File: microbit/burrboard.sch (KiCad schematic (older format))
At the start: 15 parts, among them J1 SENSORS, J2 microbit_edge_connector, J4 SPI, J6 3v3, J7 Conn_01x06, J8 I2C, J9 GND, Q1 Q_Photo_NPN, SW1 POWER_SW, U1 TMP36GT9Z

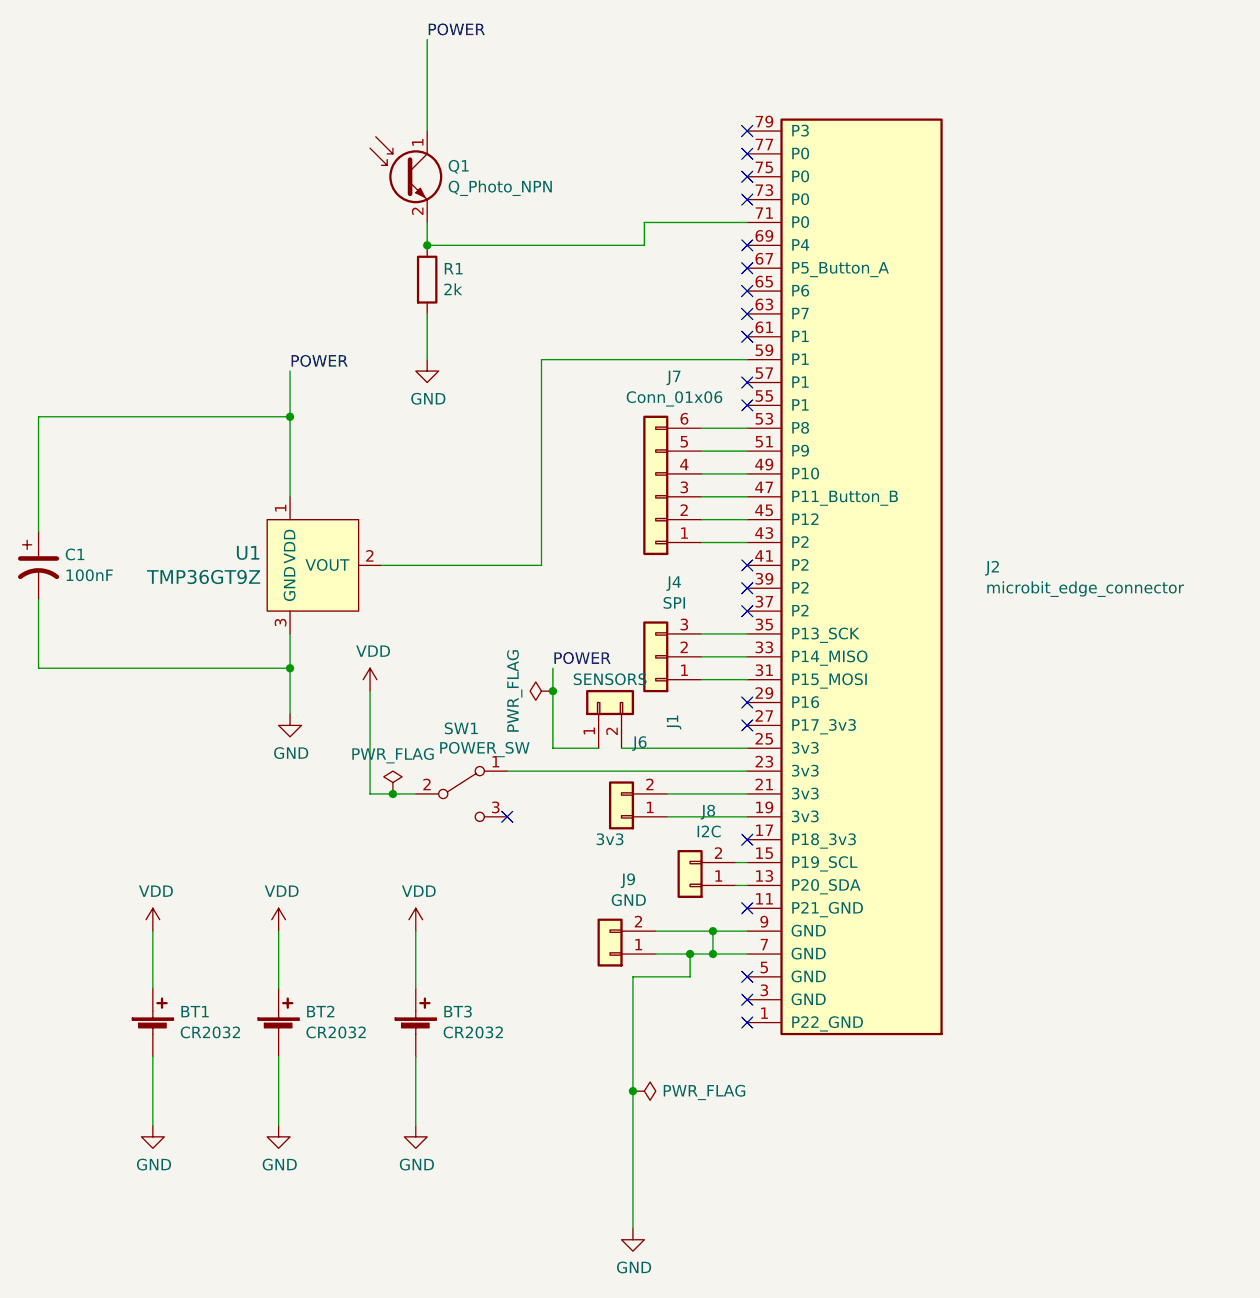
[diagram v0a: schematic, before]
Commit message: Use AAA holder
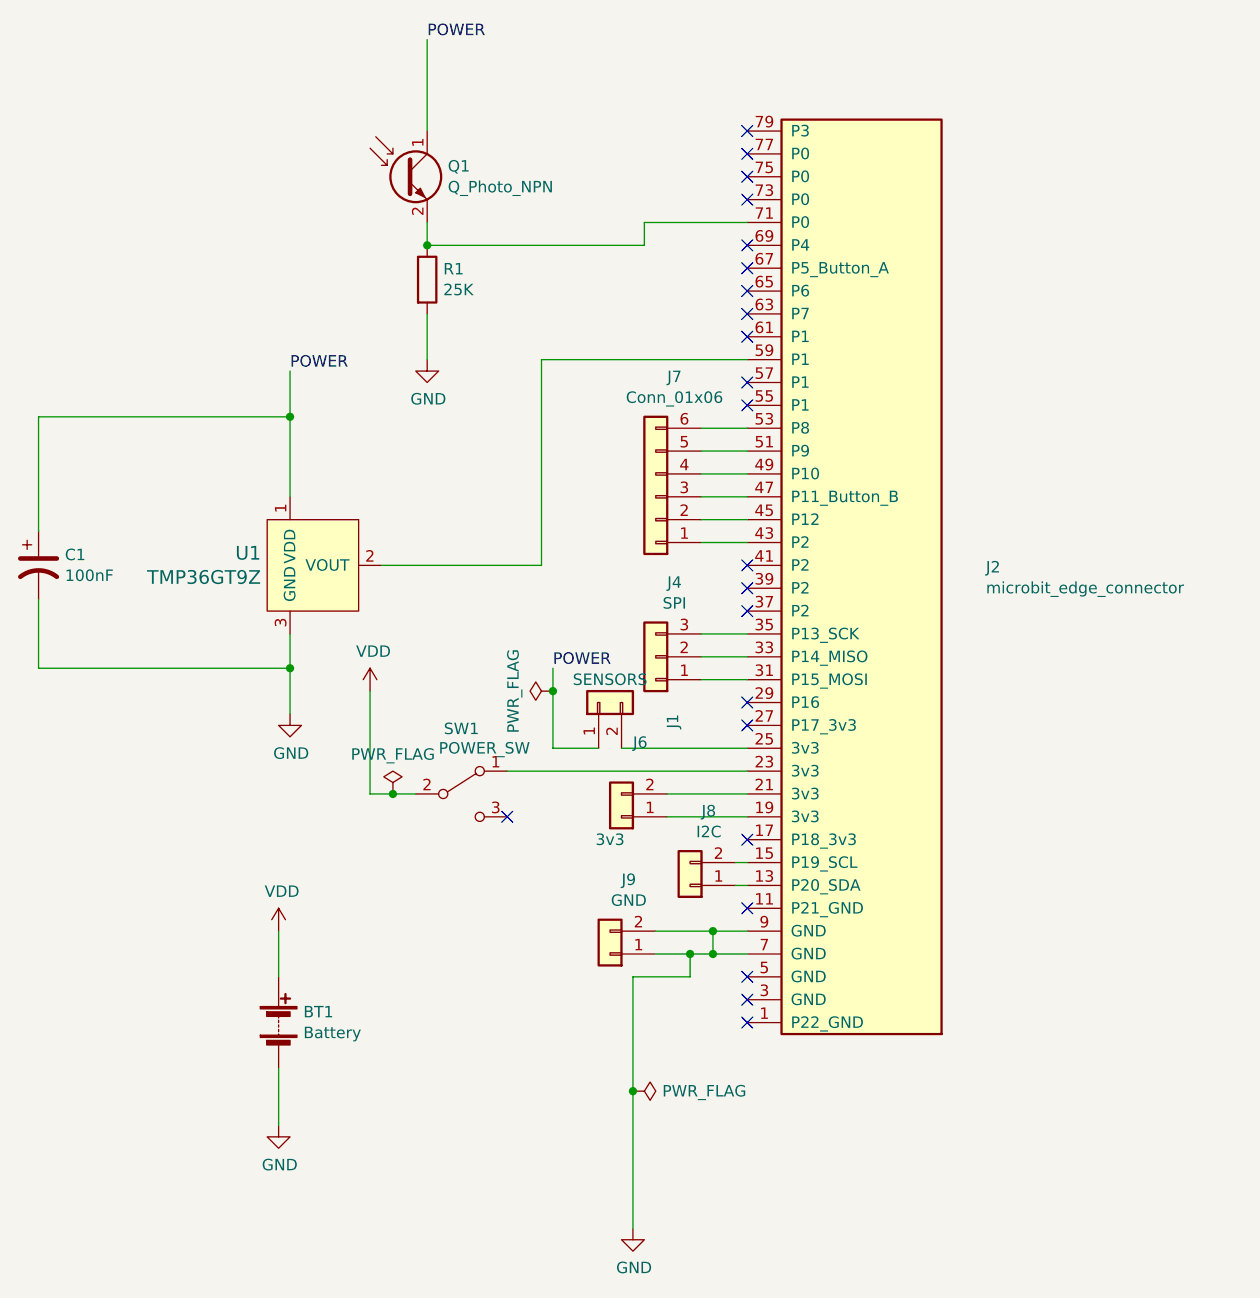
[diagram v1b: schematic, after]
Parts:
- removed BT1, BT2, BT3: CR2032, Battery:BatteryHolder_Keystone_1060_1x2032, symbol Device:Battery_Cell
- added BT1: Battery, Battery:BatteryHolder_Keystone_2468_2xAAA, symbol Device:Battery
- Q1: footprint OptoDevice:Osram_LPT80A -> burrboard:WP3DP3BT
- R1: value 2k -> 25K
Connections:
- net GND: now also BT1.2 (-)
- net VDD: now also BT1.1 (+)
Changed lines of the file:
@@
 F 0 "Q1" H 5240 2346 50  0000 L CNN
 F 1 "Q_Photo_NPN" H 5240 2255 50  0000 L CNN
-F 2 "OptoDevice:Osram_LPT80A" H 5250 2400 50  0001 C CNN
-F 3 "~" H 5050 2300 50  0001 C CNN
+F 2 "burrboard:WP3DP3BT" H 5250 2400 50  0001 C CNN
+F 3 "https://www.kingbrightusa.com/images/catalog/SPEC/WP3DP3BT.pdf" H 5050 2300 50  0001 C CNN
 	1    5050 2300
 	1    0    0    -1
@@
 P 5150 2750
 F 0 "R1" H 5220 2796 50  0000 L CNN
-F 1 "2k" H 5220 2705 50  0000 L CNN
+F 1 "25K" H 5220 2705 50  0000 L CNN
 F 2 "Resistor_THT:R_Axial_DIN0309_L9.0mm_D3.2mm_P2.54mm_Vertical" V 5080 2750 50  0001 C CNN
 F 3 "~" H 5150 2750 50  0001 C CNN
@@
 	6500 5400 6550 5400
 $Comp
-L power:GND #PWR0102
-U 1 1 61C58E75
-P 3950 6450
-F 0 "#PWR0102" H 3950 6200 50  0001 C CNN
-F 1 "GND" H 3955 6277 50  0000 C CNN
-F 2 "" H 3950 6450 50  0001 C CNN
-F 3 "" H 3950 6450 50  0001 C CNN
-	1    3950 6450
-	1    0    0    -1
-$EndComp
-$Comp
 L power:GND #PWR0105
 U 1 1 61C5B0A7
@@
 	1    0    0    -1
 $EndComp
-Wire Wire Line
-	3950 5600 3950 5850
 $Comp
 L power:GND #PWR0115
@@
 $EndComp
 $Comp
-L power:GND #PWR0116
-U 1 1 61CBB00F
-P 5100 6450
-F 0 "#PWR0116" H 5100 6200 50  0001 C CNN
-F 1 "GND" H 5105 6277 50  0000 C CNN
-F 2 "" H 5100 6450 50  0001 C CNN
-F 3 "" H 5100 6450 50  0001 C CNN
-	1    5100 6450
-	1    0    0    -1
-$EndComp
-$Comp
-L Device:Battery_Cell BT1
-U 1 1 61CCA329
-P 3950 6050
-F 0 "BT1" H 4068 6146 50  0000 L CNN
-F 1 "CR2032" H 4068 6055 50  0000 L CNN
-F 2 "Battery:BatteryHolder_Keystone_1060_1x2032" V 3950 6110 50  0001 C CNN
-F 3 "~" V 3950 6110 50  0001 C CNN
-	1    3950 6050
-	1    0    0    -1
-$EndComp
-$Comp
-L Device:Battery_Cell BT2
-U 1 1 61CCB807
-P 4500 6050
-F 0 "BT2" H 4618 6146 50  0000 L CNN
-F 1 "CR2032" H 4618 6055 50  0000 L CNN
-F 2 "Battery:BatteryHolder_Keystone_1060_1x2032" V 4500 6110 50  0001 C CNN
-F 3 "~" V 4500 6110 50  0001 C CNN
-	1    4500 6050
-	1    0    0    -1
-$EndComp
-$Comp
-L Device:Battery_Cell BT3
-U 1 1 61CCC1BE
-P 5100 6050
-F 0 "BT3" H 5218 6146 50  0000 L CNN
-F 1 "CR2032" H 5218 6055 50  0000 L CNN
-F 2 "Battery:BatteryHolder_Keystone_1060_1x2032" V 5100 6110 50  0001 C CNN
-F 3 "~" V 5100 6110 50  0001 C CNN
-	1    5100 6050
-	1    0    0    -1
-$EndComp
-Wire Wire Line
-	5100 5600 5100 5850
-Wire Wire Line
-	4500 5600 4500 5850
-Wire Wire Line
-	3950 6150 3950 6450
-Wire Wire Line
-	4500 6150 4500 6450
-Wire Wire Line
-	5100 6150 5100 6450
-$Comp
 L Device:CP1 C1
 U 1 1 61D2FCBB
@@
 	4550 3700 4550 3350
 $Comp
-L power:VDD #PWR0112
-U 1 1 61C95E4E
-P 3950 5600
-F 0 "#PWR0112" H 3950 5450 50  0001 C CNN
-F 1 "VDD" H 3965 5773 50  0000 C CNN
-F 2 "" H 3950 5600 50  0001 C CNN
-F 3 "" H 3950 5600 50  0001 C CNN
-	1    3950 5600
-	1    0    0    -1
-$EndComp
-$Comp
 L power:VDD #PWR0113
 U 1 1 61C961C8
@@
 F 3 "" H 4500 5600 50  0001 C CNN
 	1    4500 5600
-	1    0    0    -1
-$EndComp
-$Comp
-L power:VDD #PWR0114
-U 1 1 61C9662D
-P 5100 5600
-F 0 "#PWR0114" H 5100 5450 50  0001 C CNN
-F 1 "VDD" H 5115 5773 50  0000 C CNN
-F 2 "" H 5100 5600 50  0001 C CNN
-F 3 "" H 5100 5600 50  0001 C CNN
-	1    5100 5600
 	1    0    0    -1
 $EndComp
@@
 Wire Wire Line
 	6000 4800 6550 4800
+$Comp
+L Device:Battery BT1
+U 1 1 61D45279
+P 4500 6000
+F 0 "BT1" H 4608 6046 50  0000 L CNN
+F 1 "Battery" H 4608 5955 50  0000 L CNN
+F 2 "Battery:BatteryHolder_Keystone_2468_2xAAA" V 4500 6060 50  0001 C CNN
+F 3 "https://www.keyelco.com/userAssets/file/M65p28.pdf" V 4500 6060 50  0001 C CNN
+	1    4500 6000
+	1    0    0    -1
+$EndComp
+Wire Wire Line
+	4500 5600 4500 5800
+Wire Wire Line
+	4500 6200 4500 6450
 $EndSCHEMATC

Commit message: Update capacitor dimensions
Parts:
- C1: footprint Capacitor_THT:C_Disc_D7.5mm_W5.0mm_P10.00mm -> Capacitor_THT:C_Disc_D7.0mm_W2.5mm_P5.00mm
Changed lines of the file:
@@
 F 0 "C1" H 3565 4046 50  0000 L CNN
 F 1 "100nF" H 3565 3955 50  0000 L CNN
-F 2 "Capacitor_THT:C_Disc_D7.5mm_W5.0mm_P10.00mm" H 3450 4000 50  0001 C CNN
+F 2 "Capacitor_THT:C_Disc_D7.0mm_W2.5mm_P5.00mm" H 3450 4000 50  0001 C CNN
 F 3 "~" H 3450 4000 50  0001 C CNN
 	1    3450 4000
